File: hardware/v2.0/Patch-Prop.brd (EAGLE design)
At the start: 57 x 29 mm, 49 parts, among them IC1 TPS77033, IC2 ATMEGA168, IC3 MCP1253, IC5 MMA8452Q, IC6 W2RV005RM, IC7 MCP73831

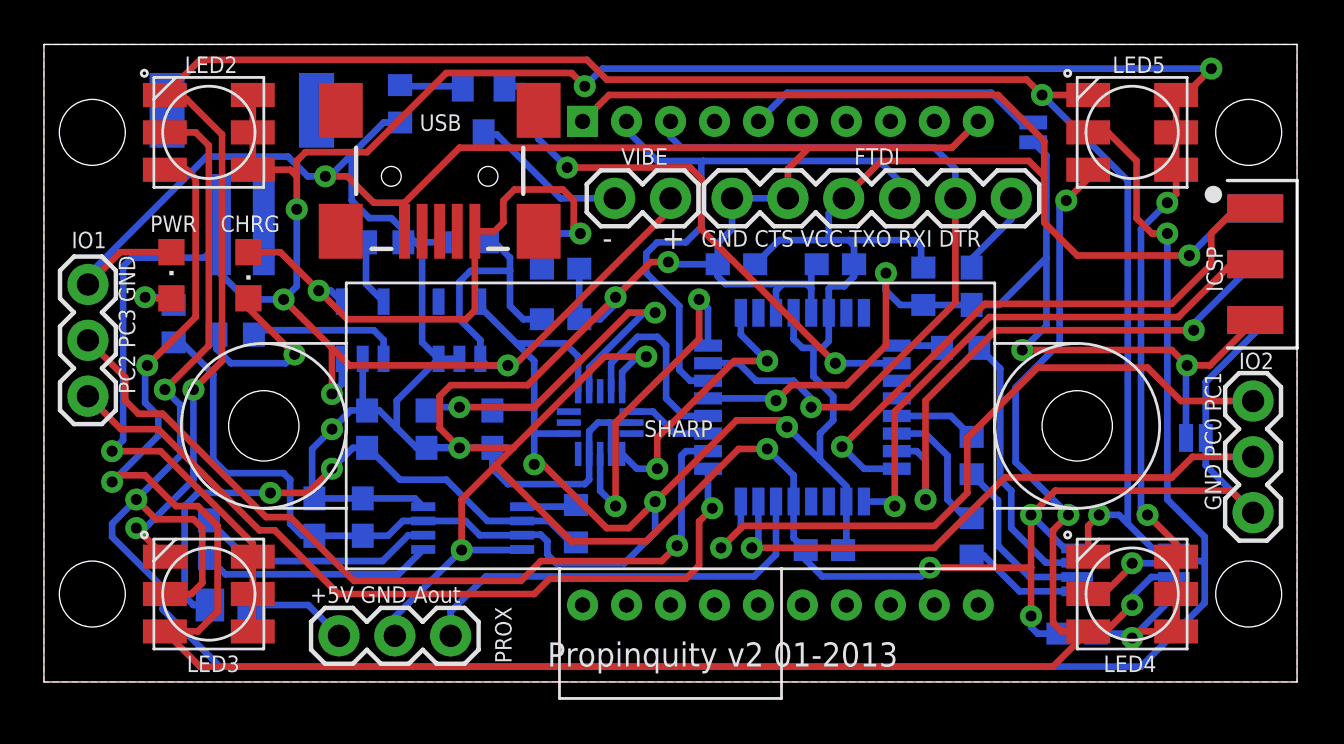
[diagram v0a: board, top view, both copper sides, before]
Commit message: Some small fixes, bigger font. First pass gerber file
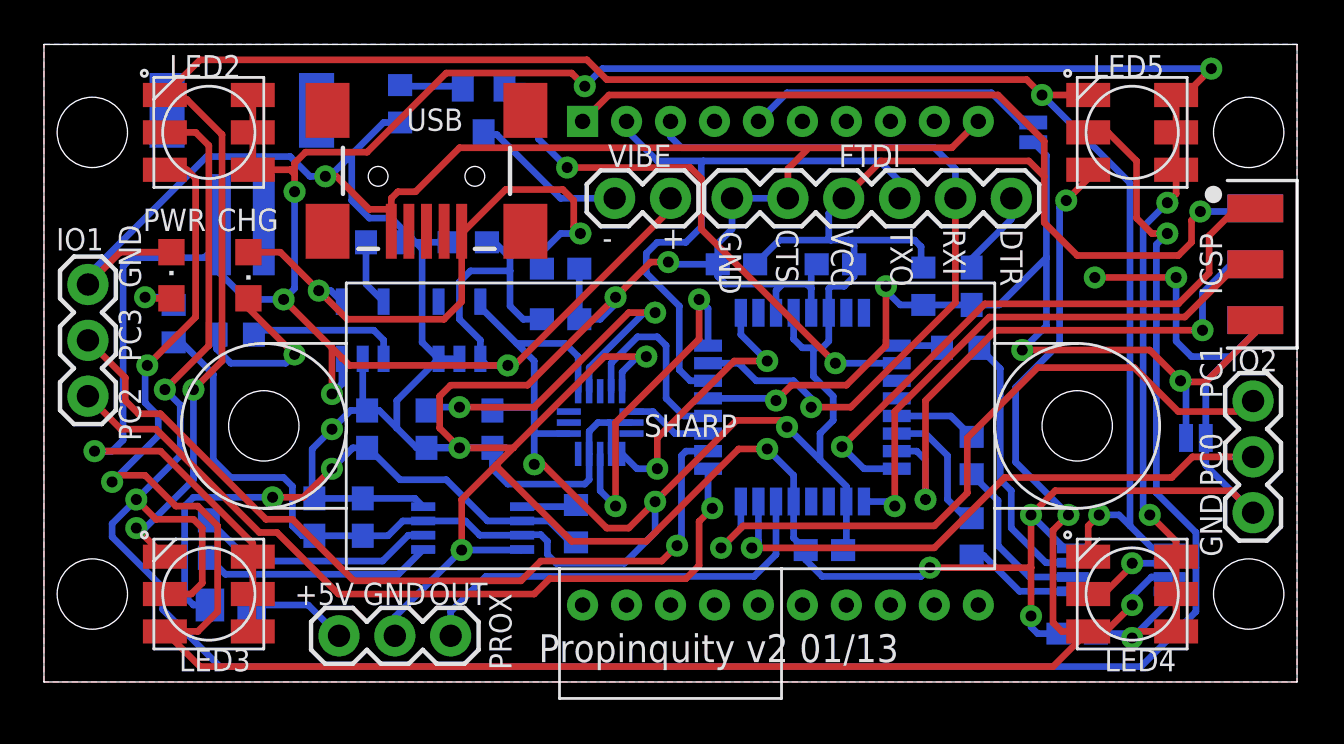
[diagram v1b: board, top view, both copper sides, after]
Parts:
- moved USB 0.60 mm to (17.4, 23.0)
- moved IC6 0.20 mm to (49.0, 5.10)
- renumbered CHRG to CHG
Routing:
- net GND: track 240.7 -> 250.6 mm, vias 11 -> 13
- net +3V3: track 143.6 -> 144.9 mm
- net V+: track 163.3 -> 164.6 mm
- net MOSI: track 25.5 -> 26.7 mm
- net RESET: track 46.9 -> 46.1 mm
- net USB_VIN: track 27.1 -> 26.3 mm
- net SCK: track 26.0 -> 25.2 mm
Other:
- board text added: "+5V"
- board text added: "CTS"
- board text added: "DTR"
- board text added: "GND"
- board text added: "OUT"
- board text added: "PC0"
- board text added: "PC1"
- board text added: "PC2"
- board text added: "PC3"
- board text added: "Propinquity v2 01/13"
- board text added: "RXI"
- board text added: "TXO"
- board text added: "VCC"
- board text removed: "+5V GND Aout"
- board text removed: "GND CTS VCC TXO RXI DTR"
- board text removed: "GND PC0 PC1"
- board text removed: "PC2 PC3 GND"
- board text removed: "Propinquity v2 01-2013"
